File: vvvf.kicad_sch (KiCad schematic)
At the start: 31 parts, among them Q1 Q_NIGBT_GCE, Q2 Q_NIGBT_GCE, Q3 Q_NIGBT_GCE, Q4 Q_NIGBT_GCE, U1 TLP152, U2 TLP152, U3 UCC21520ADW

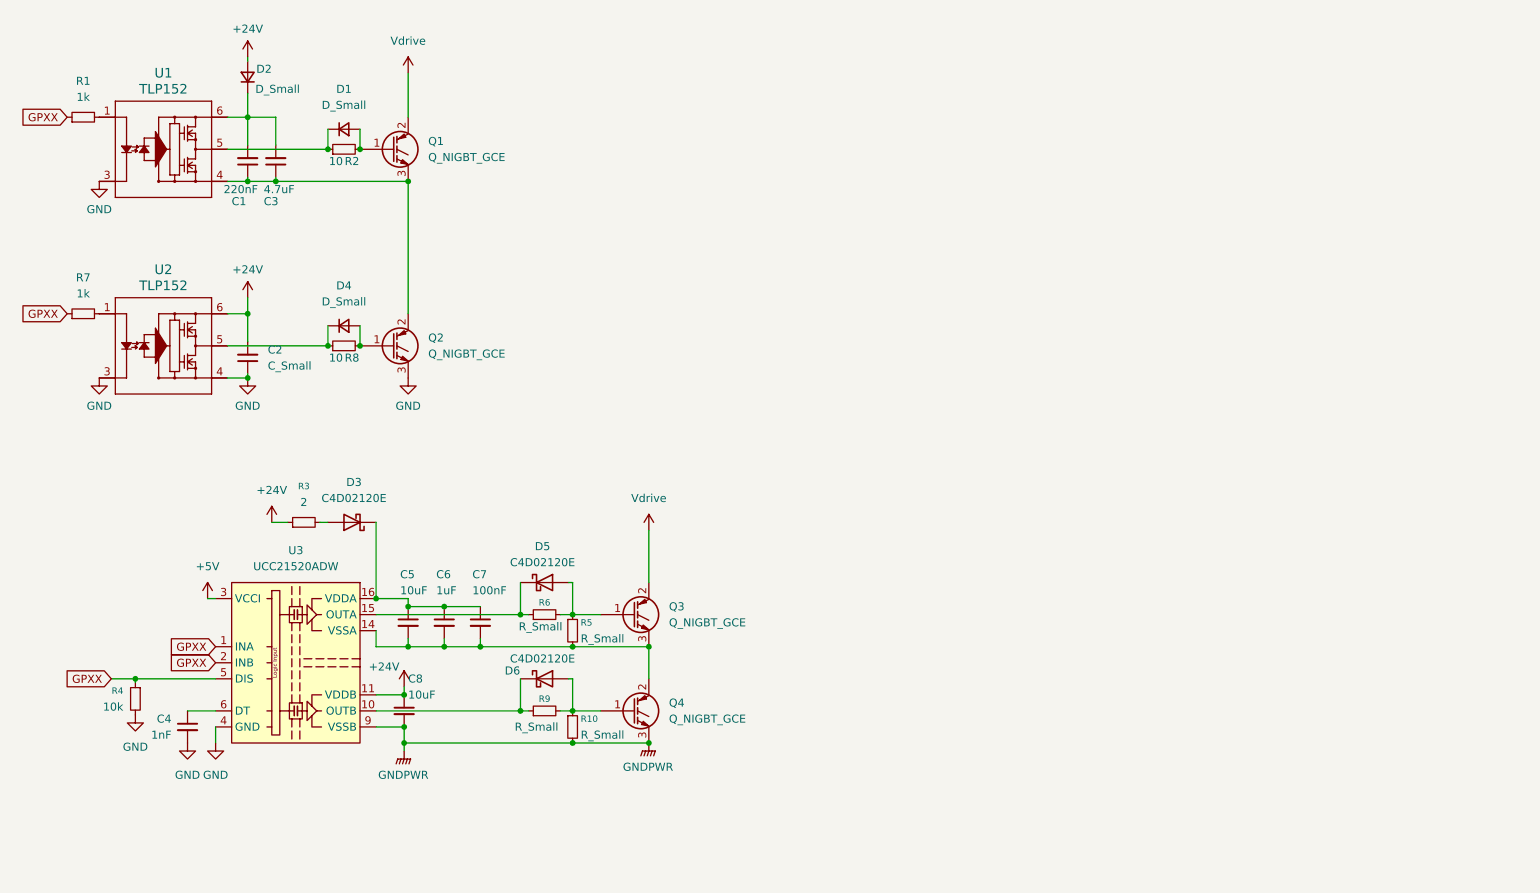
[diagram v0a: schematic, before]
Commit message: Add rpico, couple other small things
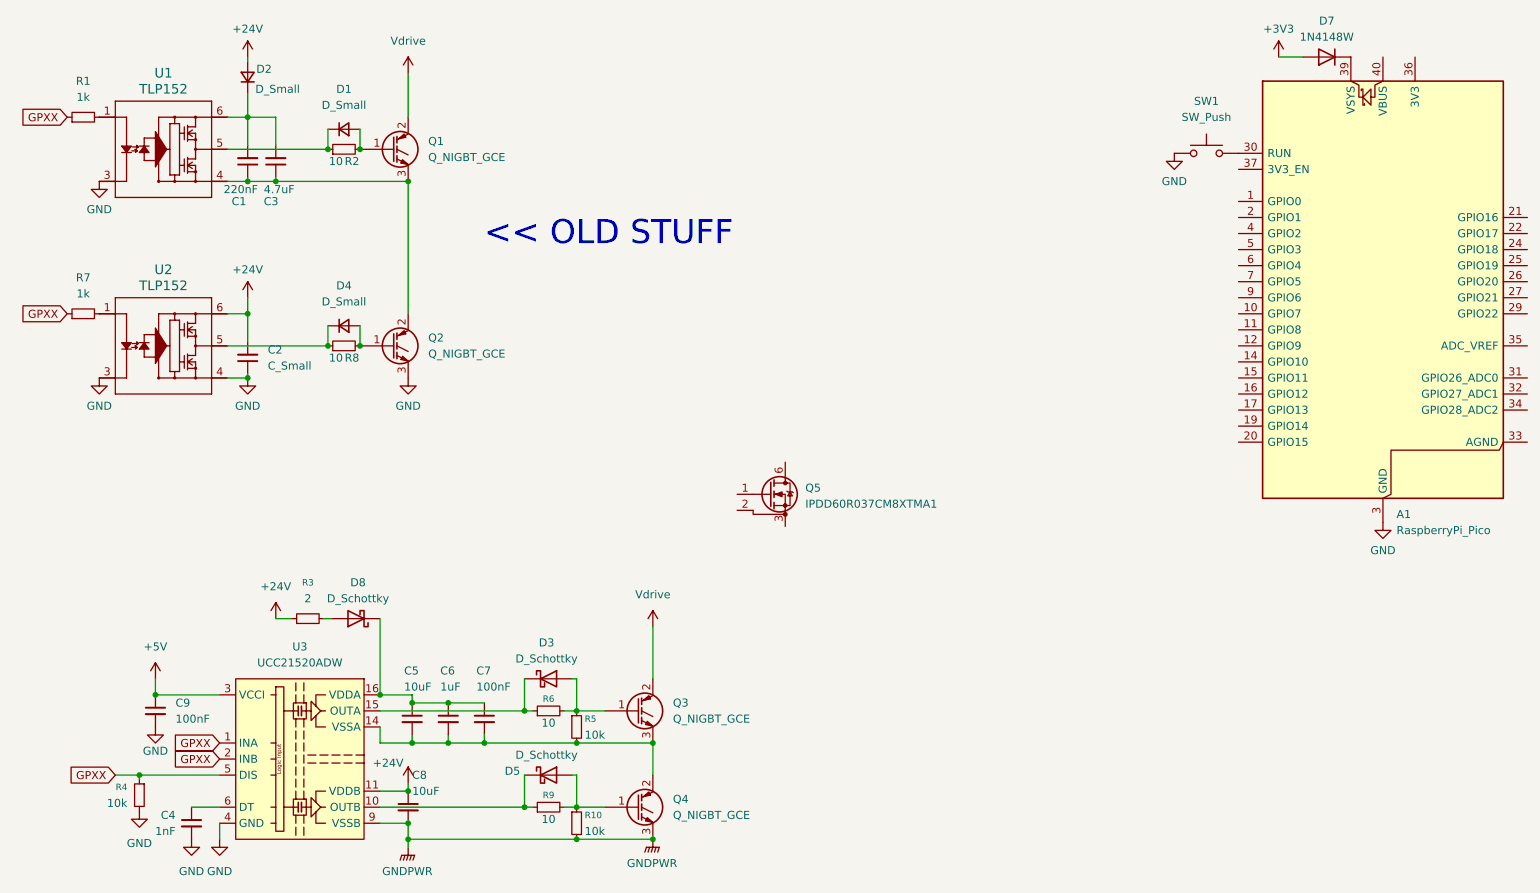
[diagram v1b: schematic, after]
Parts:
- removed D3, D5, D6: C4D02120E, Package_TO_SOT_SMD:TO-252-2_TabPin1, symbol Diode:C4D02120E
- added A1: RaspberryPi_Pico, Module:RaspberryPi_Pico_Common_Unspecified, symbol MCU_Module:RaspberryPi_Pico
- added C9: 100nF, symbol Device:C_Small
- added D3, D5, D8: D_Schottky, symbol Device:D_Schottky
- added D7: 1N4148W, Diode_SMD:D_SOD-123, symbol Diode:1N4148W
- added Q5: IPDD60R037CM8XTMA1, Package_TO_SOT_SMD:Infineon_PG-HDSOP-10-1, symbol Transistor_FET:IPDD60R050G7
- added SW1: SW_Push, symbol Switch:SW_Push
- R10, R5: value R_Small -> 10k
- R6, R9: value R_Small -> 10
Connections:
- net +5V: now also C9.1
- net GND: now also A1.13 (GND), A1.18 (GND), A1.23 (GND), A1.28 (GND), A1.3 (GND), A1.38 (GND), A1.8 (GND), C9.2, SW1.1
- net at Q3.1 (G), R5.1, R6.2: now also D3.2 (A)
- net at Q4.1 (G), R10.1, R9.2: now also D5.2 (A)
- net at C5.1, C6.1, C7.1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: now also D8.1 (K)
- net at R3.2: now also D8.2 (A)
- net at R9.1, U3.10 (OUTB): now also D5.1 (K)
- net at R6.1, U3.15 (OUTA): now also D3.1 (K)
- new net: A1.39 (VSYS), D7.1 (K)
- new net: Q5.10 (D), Q5.6 (D), Q5.7 (D), Q5.8 (D), Q5.9 (D)
- new net: Q5.3 (PS), Q5.4 (PS), Q5.5 (PS)
- new net: A1.30 (RUN), SW1.2
- new net +3V3: D7.2 (A)
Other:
- note added: "<< OLD STUFF"
- moved on the sheet: C4, C5, C6, C7, C8, Q3, Q4, R10, R3, R4, R5, R6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

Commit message: Add brake chopper
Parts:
- removed Q3, Q4: Q_NIGBT_GCE, symbol Device:Q_NIGBT_GCE
- added D6: D_Schottky, symbol Device:D_Schottky
- added Q3, Q4: IPDD60R037CM8XTMA1, Package_TO_SOT_SMD:Infineon_PG-HDSOP-10-1, symbol Transistor_FET:IPDD60R050G7
- added R11: 10, symbol Device:R_Small
- added R12: 10k, symbol Device:R_Small
- added R13: 6, symbol Device:R_Small
- added U4: TLP152, 5pin SO6_TOS, symbol TLP152:TLP152
- C1, C2, C3, D1, D2, D4, Q1, Q2, R1, R2, R7, R8, U1, U2: now not fitted; now left out of the parts list
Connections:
- net +24V: now also U4.6
- net GND: now also A1.33 (AGND), Q4.2 (DS), Q4.3 (PS), Q4.4 (PS), Q4.5 (PS), R12.2, U4.3, U4.4
- net GNDPWR: now also Q3.2 (DS), Q3.3 (PS), Q3.4 (PS), Q3.5 (PS)
- net GPXX: now also U4.1; no longer R7.1
- net Vdrive: now also Q5.10 (D), Q5.6 (D), Q5.7 (D), Q5.8 (D), Q5.9 (D), R13.1
- net at D3.2 (A), R5.1, R6.2: now also Q5.1 (G)
- net at C5.2, C6.2, C7.2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: now also Q5.2 (DS)
- net at D5.2 (A), R10.1, R9.2: now also Q3.1 (G)
- net at Q5.3 (PS), Q5.4 (PS), Q5.5 (PS): now also Q3.10 (D), Q3.6 (D), Q3.7 (D), Q3.8 (D), Q3.9 (D)
- new net: D6.2 (A), Q4.1 (G), R11.2, R12.1
- new net: Q4.10 (D), Q4.6 (D), Q4.7 (D), Q4.8 (D), Q4.9 (D), R13.2
- new net: D6.1 (K), R11.1, U4.5
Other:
- note added: "VVVF Inverter"
- moved on the sheet: A1, C4, C5, C6, C7, C8, C9, D3, D5, D7, D8, Q5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

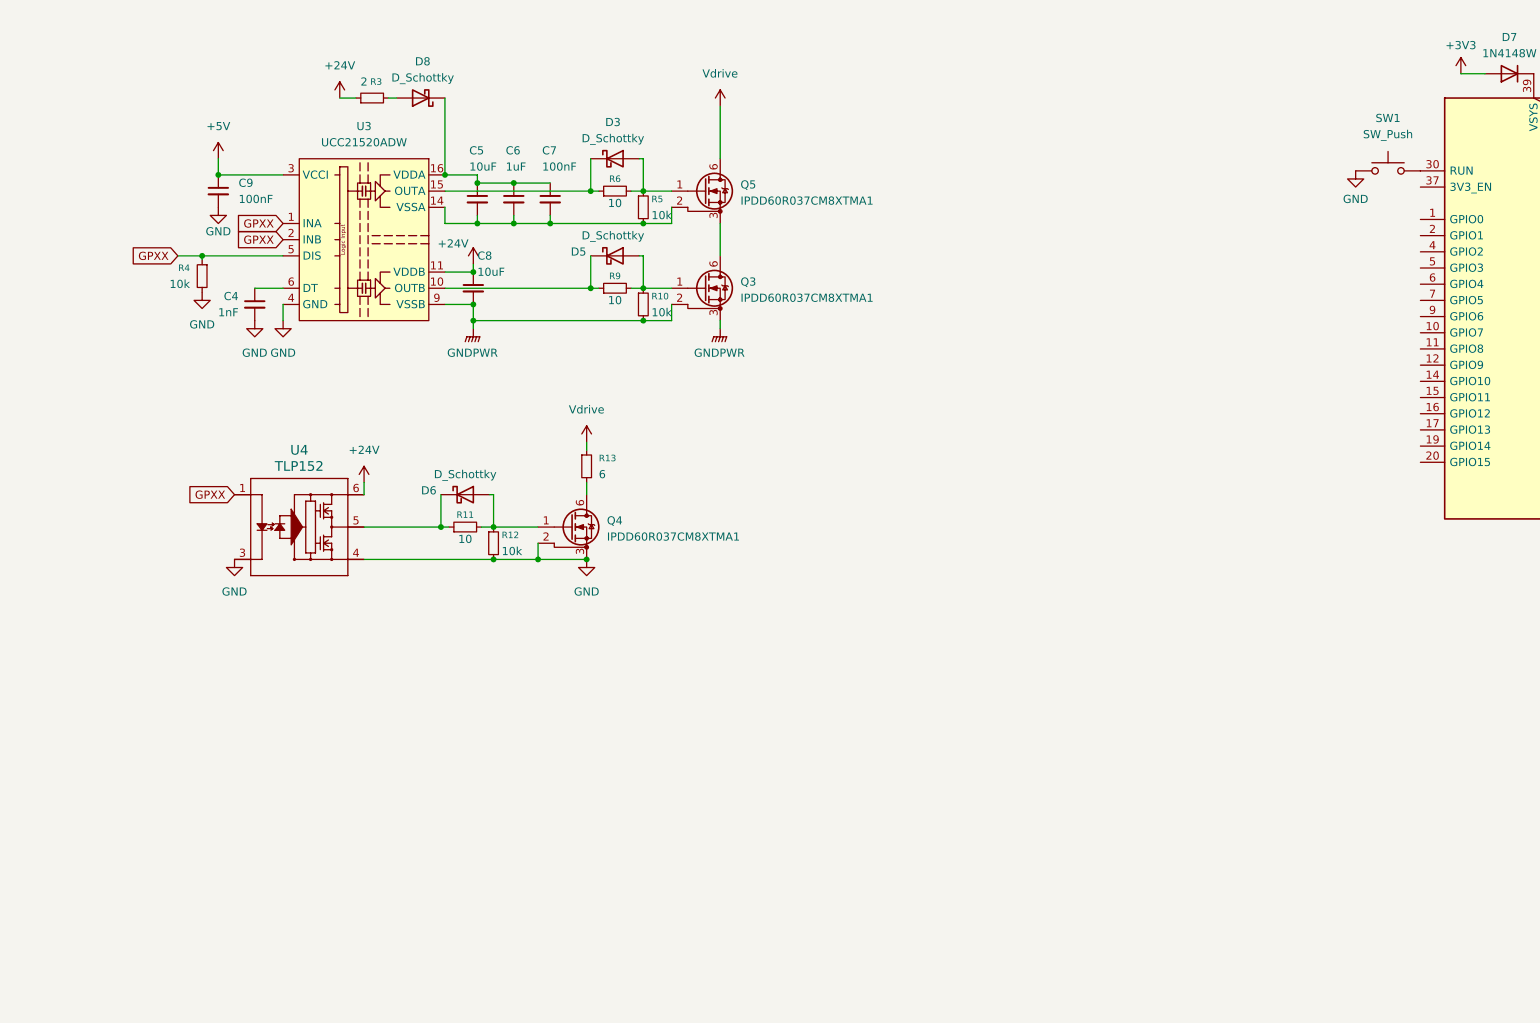
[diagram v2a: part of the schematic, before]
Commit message: Add current sensing
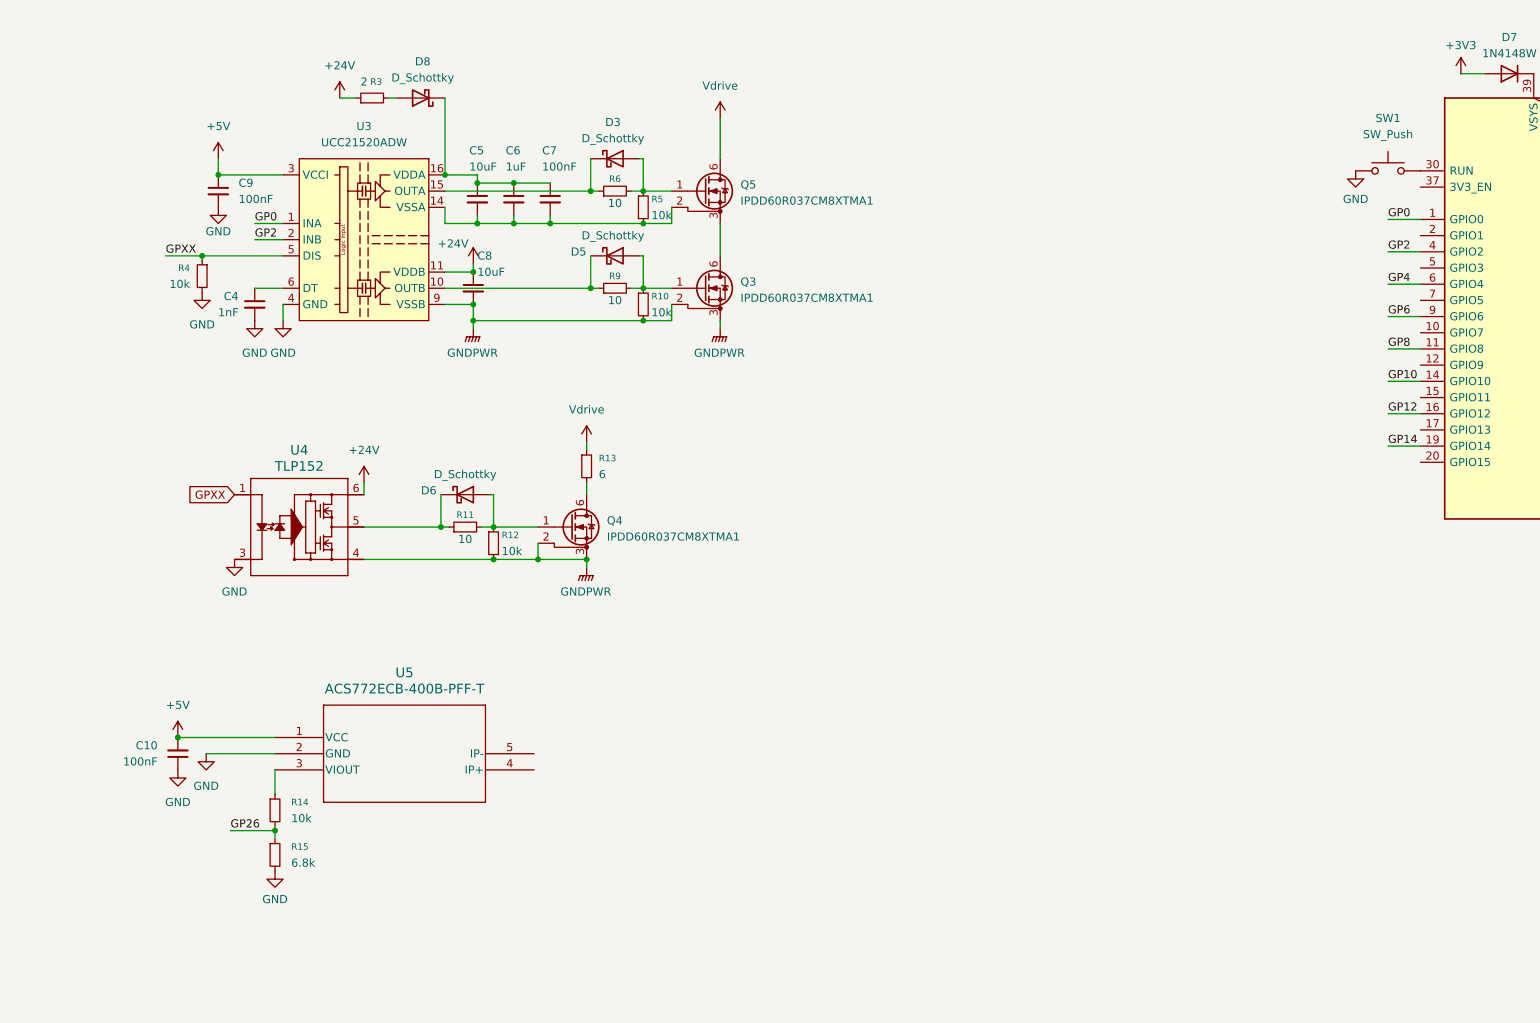
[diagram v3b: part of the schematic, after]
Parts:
- added C10: 100nF, symbol Device:C_Small
- added R14: 10k, symbol Device:R_Small
- added R15: 6.8k, symbol Device:R_Small
- added U5: ACS772ECB-400B-PFF-T, Snapeda:ACS772_PFF_ALM, symbol Snapeda:ACS772ECB-400B-PFF-T
- Q3, Q4, Q5: Digikey Part (none) -> 448-IPDD60R037CM8XTMA1CT-ND
- U3: Digikey Part (none) -> 296-48796-1-ND
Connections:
- net +5V: now also C10.2, U5.1 (VCC)
- net GND: now also C10.1, R15.2, U5.2 (GND); no longer Q4.2 (DS), Q4.3 (PS), Q4.4 (PS), Q4.5 (PS), R12.2, U4.4
- net GNDPWR: now also Q4.2 (DS), Q4.3 (PS), Q4.4 (PS), Q4.5 (PS), R12.2, U4.4
- net GPXX: no longer U3.1 (INA), U3.2 (INB)
- net GP0: now reaches A1.1 (GPIO0)
- net GP0: now also U3.1 (INA)
- net GP8: now reaches A1.11 (GPIO8)
- net GP10: now reaches A1.14 (GPIO10)
- net GP12: now reaches A1.16 (GPIO12)
- net GP14: now reaches A1.19 (GPIO14)
- net GP2: now reaches A1.4 (GPIO2)
- net GP2: now also U3.2 (INB)
- net GP4: now reaches A1.6 (GPIO4)
- net GP6: now reaches A1.9 (GPIO6)
- new net: R14.1, U5.3 (VIOUT)
- new net GP26: R14.2, R15.1
